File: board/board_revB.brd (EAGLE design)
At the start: 94 x 44.5 mm, 81 parts, among them Q2 ULN2003AD, Y1 8Mhz

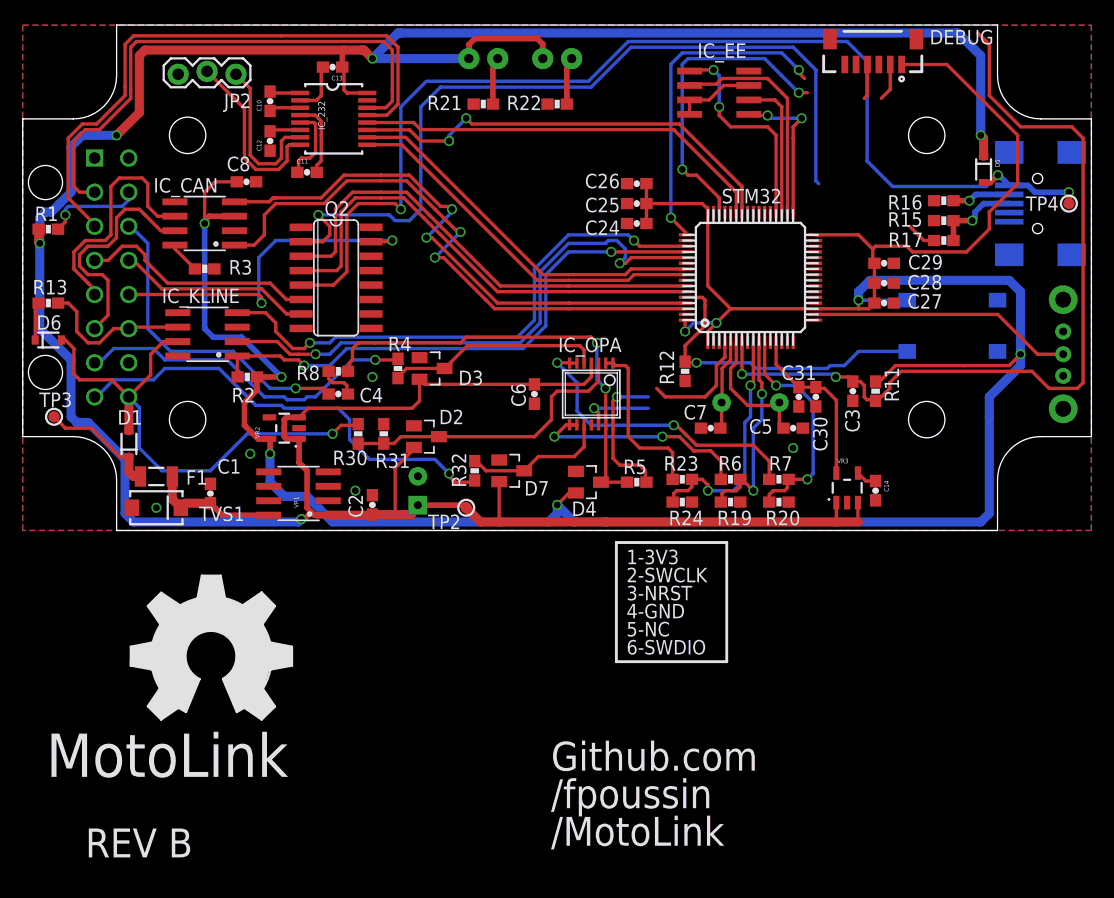
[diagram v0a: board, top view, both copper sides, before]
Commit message: [Board] working on rev B (routing)
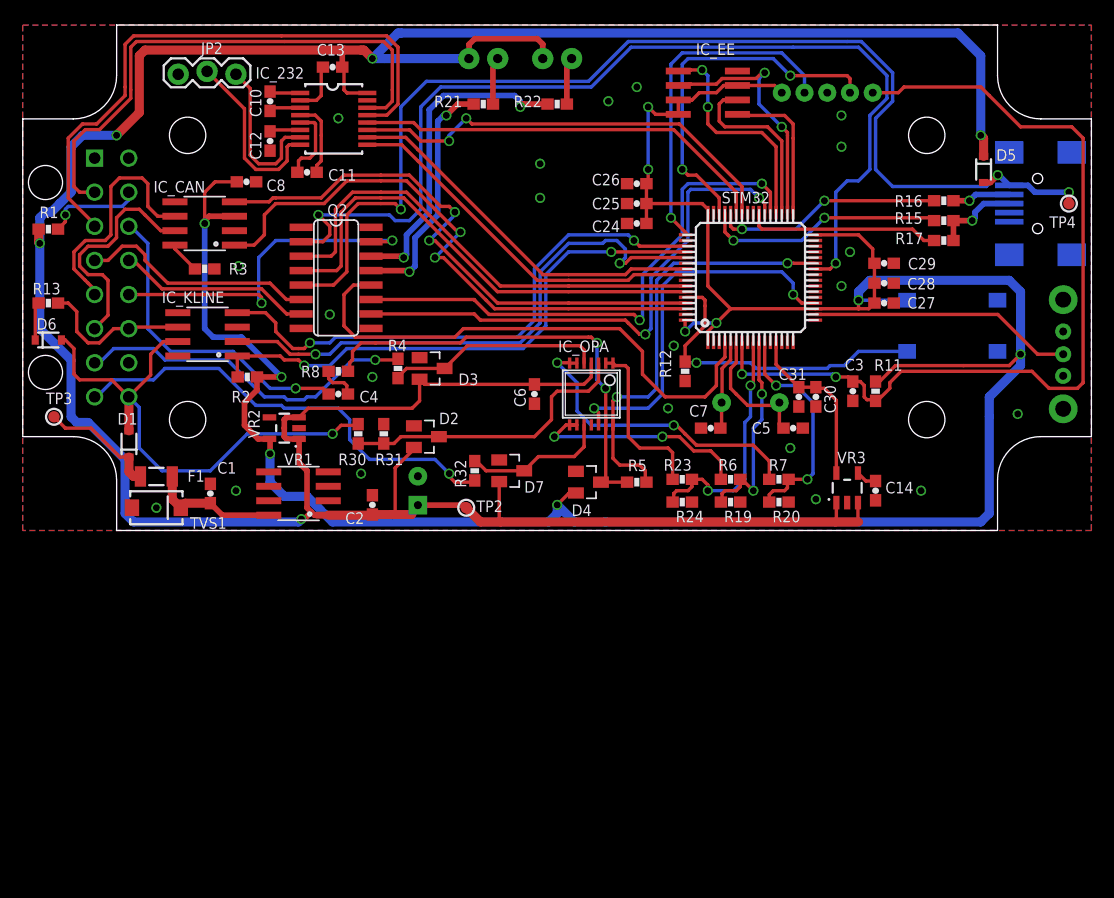
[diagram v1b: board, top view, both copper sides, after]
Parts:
- removed CON_DBG: JST_VERTICAL, SparkFun-Connectors:JST-6-SMD-VERT-1.0MM
- added JP4: (no value), SparkFun-Connectors:JST-5-PTH
- moved U$6 52.1 mm to (40.0, 25.6), flipped to the bottom
- moved IC_EE 1.00 mm to (60.2, 38.5)
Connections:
- removed net SWO: CON_DBG.6
- net +3V3: now also JP4.5; no longer CON_DBG.1
- net GND: now also JP4.3; no longer CON_DBG.3
- net NRST: now also JP4.1; no longer CON_DBG.5
- net SWCLK: now also JP4.4; no longer CON_DBG.2
- net SWDIO: now also JP4.2; no longer CON_DBG.4
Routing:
- net FREQ1_IN: track 0.00 -> 47.5 mm, vias 0 -> 2
- net FREQ2_IN: track 0.00 -> 47.1 mm, vias 0 -> 2
- net USB_DETECT: track 10.1 -> 47.1 mm
- net N$15: track 0.00 -> 28.6 mm, vias 0 -> 2
- net DAC1: track 6.38 -> 33.3 mm, vias 1 -> 2
- net KNK_AN: track 12.6 -> 37.8 mm, vias 1 -> 2
- net N$11: track 0.00 -> 21.5 mm, vias 0 -> 2
- net USB_DP: track 0.00 -> 21.3 mm, vias 0 -> 2
- net USB_DM: track 0.00 -> 20.2 mm, vias 0 -> 2
- net +3V3: track 254.4 -> 234.8 mm, vias 8 -> 10
- net SCS_TRIG: track 71.4 -> 88.7 mm, vias 1 -> 2
- net USB_CTRL: track 2.67 -> 17.1 mm
- net NRST: track 73.8 -> 78.6 mm
- net SPI2_MISO: track 12.5 -> 15.8 mm
- net SWCLK: track 32.1 -> 30.0 mm, vias 2 -> 1
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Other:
- board text removed: "1-3V3"
- board text removed: "2-SWCLK"
- board text removed: "3-NRST"
- board text removed: "4-GND"
- board text removed: "5-NC"
- board text removed: "6-SWDIO"

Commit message: [Board] working on rev B (routing/schema)
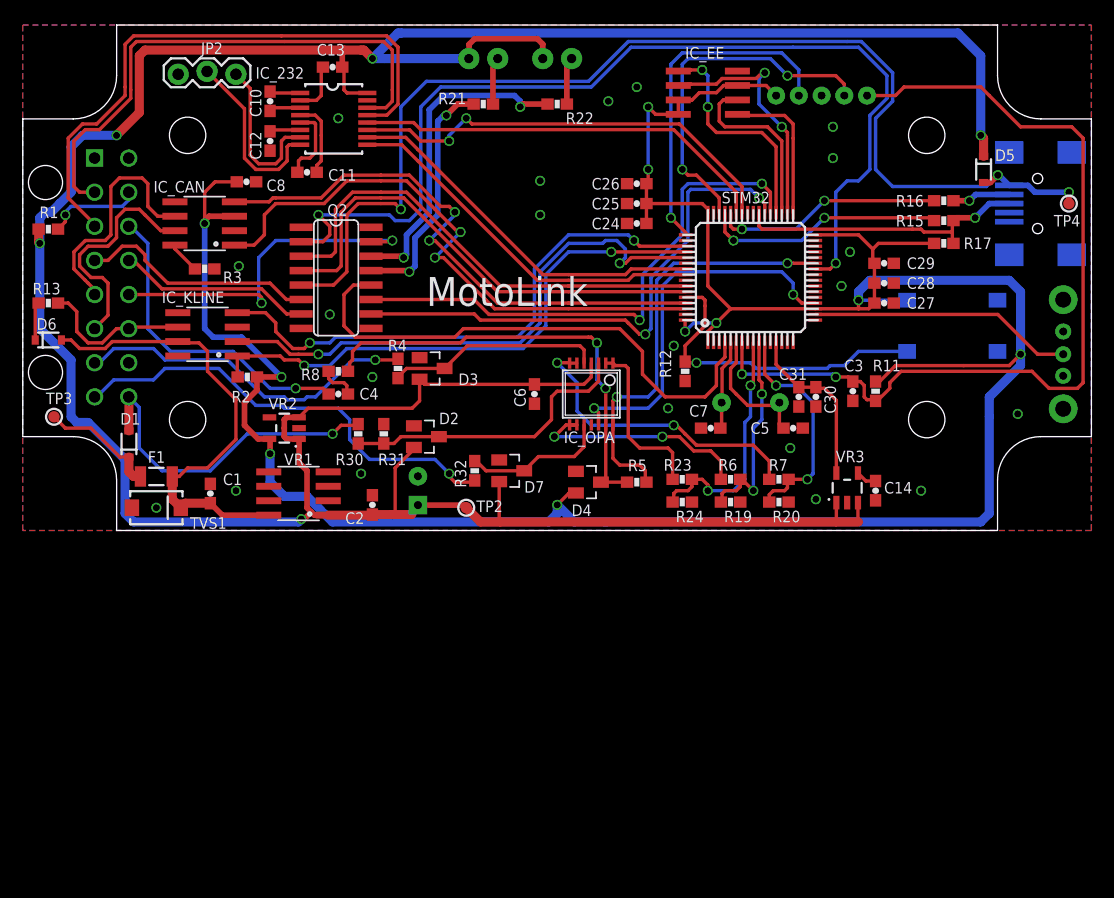
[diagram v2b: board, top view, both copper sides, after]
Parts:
- C9: value 47uF 25v -> 100uF 16v
- IC_KLINE: value MCP2004 -> TJA1027
- moved JP4 0.56 mm to (70.2, 38.2)
- moved R17 0.25 mm to (81.0, 25.2)
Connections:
- removed net N$7: JP1.D+, R15.1, R17.2
- net +12V: no longer D6.2, IC_KLINE.7
- net +3V3: now also R17.1
- net USB_CTRL: now also JP1.D+, R15.1, R17.2; no longer R17.1
- net VCC_PROT: now also D6.2, IC_KLINE.7
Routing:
- net VCC_PROT: track 11.4 -> 40.9 mm
- net +12V: track 46.4 -> 29.7 mm
- net USB_CTRL: track 17.1 -> 26.2 mm, vias 0 -> 1
- net N$7: track 7.56 -> 0.00 mm, vias 1 -> 0
- net +3V3: track 234.8 -> 240.0 mm
- net NRST: track 78.6 -> 79.2 mm
- net SWDIO: track 31.8 -> 31.2 mm
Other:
- board text added: "BOOT0"

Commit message: [Board] working on rev B (routing)
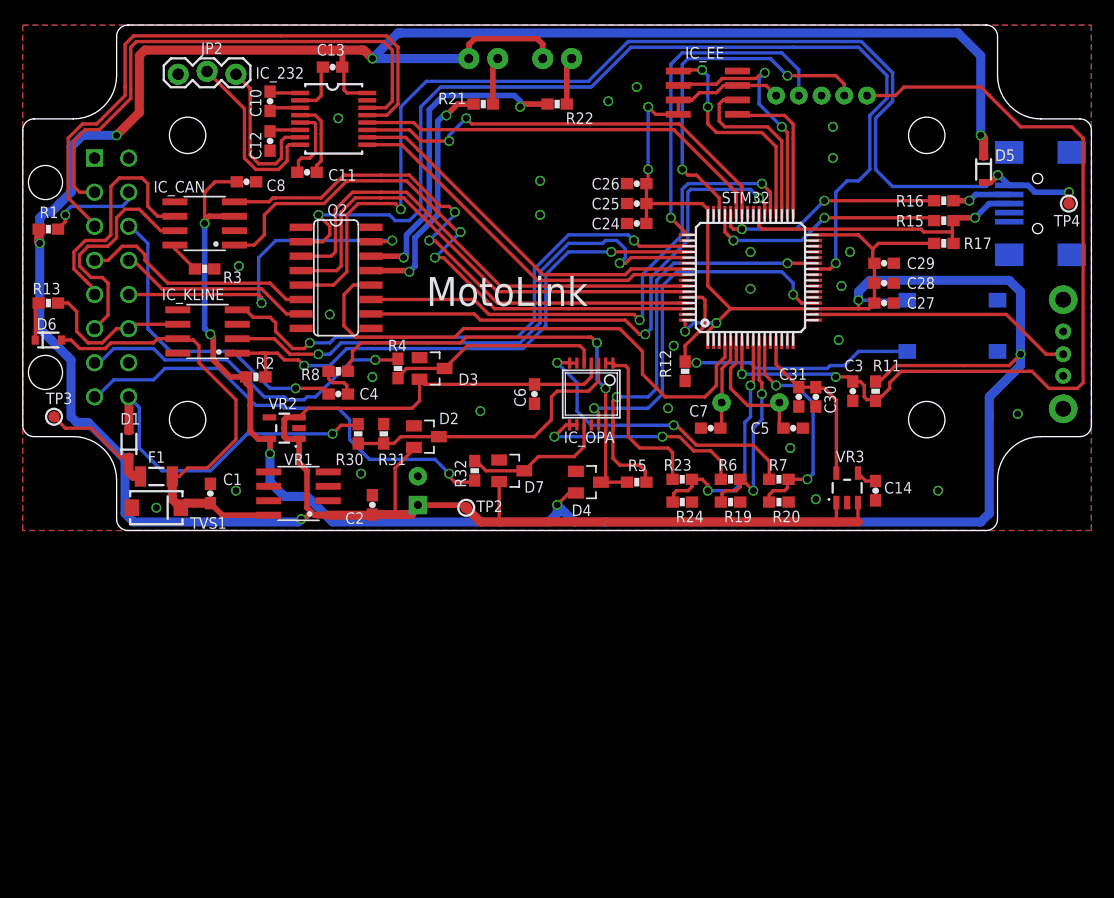
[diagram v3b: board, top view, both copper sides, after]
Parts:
- moved R2 0.75 mm to (20.5, 13.5), turned to 180 degrees
- moved IC_KLINE 0.25 mm to (16.2, 17.5)
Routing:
- net +3V3: track 240.0 -> 235.4 mm
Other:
- outline, holes or cut-outs redrawn

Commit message: [Board] working on rev B (routing/cleaning)
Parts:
- removed S2: EG1213, adafruit:EG1213
- added S3: (no value), SparkFun-Electromechanical:TACTILE-PTH-SIDEEZ
- JP1: value USBSMD -> USB-B; device SparkFun-Connectors:USB-MINIB -> SparkFun-Connectors:USB-B-PTH
- moved JP4 12.0 mm to (58.2, 38.2)
- moved IC_EE 9.28 mm to (69.5, 37.8)
- moved S1 6.27 mm to (75.5, 17.5)
- moved TP4 4.61 mm to (91.0, 24.2)
- moved JP1 3.95 mm to (86.0, 26.5)
- moved R3 1.03 mm to (17.0, 23.2)
- moved D3 0.25 mm to (36.0, 14.0)
- moved R21 0.25 mm to (40.5, 37.8)
- moved R22 0.25 mm to (47.0, 37.8)
- moved R4 0.25 mm to (33.0, 14.0)
- flipped LED1 to the top, turned to 0 degrees
- flipped LED2 to the top, turned to 0 degrees
- renumbered JP2 to CON_RS232
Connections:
- new net VCC_DETECT: Q2.16, STM32.57
- net BUT1: now also S3.1; no longer S2.2
- net GND: now also S3.2; no longer S2.3
- net VCC_PROT: now also Q2.1
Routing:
- net VCC_DETECT: track 0.00 -> 33.2 mm, vias 0 -> 2
- net NRST: track 79.2 -> 97.9 mm
- net VCC_PROT: track 41.0 -> 59.3 mm, vias 0 -> 2
- net SWDIO: track 31.2 -> 13.0 mm, vias 2 -> 1
- net SWCLK: track 30.1 -> 13.1 mm
- net SPI2_SCK: track 21.6 -> 13.4 mm
- net +5V: track 281.0 -> 273.5 mm
- net BOOT0: track 28.3 -> 22.1 mm
- net SPI2_MOSI: track 19.7 -> 13.9 mm
- net USB_VBUS: track 100.9 -> 105.4 mm, vias 3 -> 2
- net +3V3: track 235.4 -> 231.2 mm, vias 10 -> 9
- net SPI2_MISO: track 15.8 -> 12.4 mm
- net SPI2_NSS: track 13.0 -> 9.70 mm
- net BUT1: track 23.2 -> 25.9 mm
- net N$17: track 5.13 -> 2.69 mm, vias 1 -> 0
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
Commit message: [Board] working on rev B (routing/cleaning)
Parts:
- flipped CON_RS232 to the bottom, turned to 0 degrees
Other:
- board text added: "GND"
- board text added: "RS232"
- board text added: "RX"
- board text added: "TX"
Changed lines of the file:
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@@
 <text x="77.75" y="21.25" size="1.016" layer="26" font="vector" ratio="12" rot="MR0">BOOT0</text>
 <text x="32.5" y="18.5" size="3.81" layer="25" font="vector" ratio="12">MotoLink</text>
+<text x="14.75" y="42" size="1.016" layer="22" font="vector" ratio="12" rot="MR0">GND</text>
+<text x="17" y="42" size="1.016" layer="22" font="vector" ratio="12" rot="MR0">RX</text>
+<text x="19.75" y="42" size="1.016" layer="22" font="vector" ratio="12" rot="MR0">TX</text>
+<text x="20.5" y="40.75" size="1.016" layer="22" font="vector" ratio="12" rot="MR180">RS232</text>
 </plain>
 <attributes>
@@
 </element>
 <element name="IC_232" library="SparkFun-DigitalIC" package="TSSOP16" value="MAX202" x="27.25" y="36.25" locked="yes" smashed="yes" rot="R270">
-<attribute name="NAME" x="20.476" y="39.73" size="1.016" layer="25" font="vector" ratio="12"/>
+<attribute name="NAME" x="29.226" y="39.73" size="1.016" layer="25" font="vector" ratio="12"/>
 <attribute name="VALUE" x="28.139" y="37.774" size="0.6096" layer="27" rot="R270"/>
 </element>
@@
 </element>
 <element name="X2" library="con-molex-micro-fit-3_0" package="43045-1600" value="" x="2" y="22.25" locked="yes" smashed="yes" rot="MR90"/>
-<element name="CON_RS232" library="SparkFun-Connectors" package="1X03_LOCK" value="" x="18.75" y="40.25" smashed="yes" rot="R180">
-<attribute name="NAME" x="12.1538" y="42.0788" size="1.016" layer="25" font="vector" ratio="12"/>
-<attribute name="VALUE" x="20.02" y="43.425" size="1.27" layer="27" rot="R180"/>
+<element name="CON_RS232" library="SparkFun-Connectors" package="1X03_LOCK" value="" x="18.75" y="40.25" smashed="yes" rot="MR0">
+<attribute name="VALUE" x="20.02" y="37.075" size="1.27" layer="28" rot="MR0"/>
 </element>
 <element name="D5" library="SparkFun-DiscreteSemi" package="SOD-323" value="BAT165" x="84.5" y="31.75" smashed="yes" rot="R270">
@@
 <wire x1="69.7" y1="19.5" x2="62.25" y2="19.5" width="0.3" layer="1"/>
 <wire x1="62.25" y1="19.5" x2="61" y2="18.25" width="0.3" layer="1"/>
-<wire x1="54.85" y1="30.5" x2="54.85" y2="28.75" width="0.3" layer="1"/>
-<wire x1="54.85" y1="27" x2="54.85" y2="28.75" width="0.3" layer="1"/>
+<wire x1="54.85" y1="30.5" x2="54.85" y2="28.75" width="0.5" layer="1"/>
+<wire x1="54.85" y1="27" x2="54.85" y2="28.75" width="0.5" layer="1"/>
 <wire x1="60.25" y1="27.95" x2="60.25" y2="28.25" width="0.3" layer="1"/>
 <wire x1="60.25" y1="28.25" x2="59.75" y2="28.75" width="0.3" layer="1"/>
@@
 <wire x1="60.25" y1="27.95" x2="60.25" y2="21.5" width="0.3" layer="1"/>
 <wire x1="60.25" y1="21.5" x2="62.25" y2="19.5" width="0.3" layer="1"/>
-<wire x1="55" y1="36.5" x2="55" y2="31.75" width="0.3" layer="16"/>
+<wire x1="55" y1="36.5" x2="55" y2="31.75" width="0.5" layer="16"/>
 <via x="55" y="31.75" extent="1-16" drill="0.6"/>
-<wire x1="55" y1="31.75" x2="55" y2="30.65" width="0.3" layer="1"/>
+<wire x1="55" y1="31.75" x2="55" y2="30.65" width="0.5" layer="1"/>
 <wire x1="55" y1="30.65" x2="54.85" y2="30.5" width="0.3" layer="1"/>
 <contactref element="JP4" pad="5"/>
@@
 <wire x1="20.5" y1="31.75" x2="19.5" y2="32.75" width="0.3" layer="1"/>
 <wire x1="19.5" y1="32.75" x2="19.5" y2="37.087" width="0.3" layer="1"/>
-<wire x1="19.5" y1="37.087" x2="16.21" y2="40.377" width="0.3" layer="1"/>
+<wire x1="16.21" y1="40.123" x2="16.464" y2="40.123" width="0.3" layer="1"/>
+<wire x1="16.464" y1="40.123" x2="19.5" y2="37.087" width="0.3" layer="1"/>
 </signal>
 <signal name="UART2_TXD_232">
@@
 <wire x1="20.75" y1="32.25" x2="20" y2="33" width="0.3" layer="1"/>
 <wire x1="20" y1="33" x2="20" y2="38.873" width="0.3" layer="1"/>
-<wire x1="20" y1="38.873" x2="18.75" y2="40.123" width="0.3" layer="1"/>
+<wire x1="18.75" y1="40.377" x2="18.75" y2="40.123" width="0.3" layer="1"/>
+<wire x1="18.75" y1="40.123" x2="20" y2="38.873" width="0.3" layer="1"/>
 </signal>
 <signal name="UART3_TX">

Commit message: [Board] working on rev B (routing/cleaning)
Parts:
- removed JP4: (no value), SparkFun-Connectors:JST-5-PTH
- added X1: JST-ZH, con-jst:S4B-ZR
- moved C27 1.50 mm to (74.2, 20.0)
- moved C28 1.50 mm to (74.2, 21.8)
- moved C29 1.50 mm to (74.2, 23.5)
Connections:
- net +3V3: no longer JP4.5
- net GND: now also X1.2; no longer JP4.3
- net NRST: now also X1.4; no longer JP4.1
- net SWCLK: now also X1.1; no longer JP4.4
- net SWDIO: now also X1.3; no longer JP4.2
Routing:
- net SWCLK: track 13.1 -> 14.6 mm
- net SWDIO: track 13.0 -> 14.1 mm
- net +3V3: track 231.2 -> 230.8 mm, vias 9 -> 10

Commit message: [Board] working on rev B (routing/cleaning)
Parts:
- IC_EE: value FM25L04B -> FM25L04B/AT24C256
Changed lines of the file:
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@@
 <attribute name="PROD_ID" value="RES-11150" x="11.75" y="4.75" size="1.778" layer="27" rot="R180" display="off"/>
 </element>
-<element name="IC_EE" library="microchip" package="SO-08" value="FM25L04B" x="69.5" y="37.75" smashed="yes" rot="R90">
+<element name="IC_EE" library="microchip" package="SO-08" value="FM25L04B/AT24C256" x="69.5" y="37.75" locked="yes" smashed="yes" rot="R90">
 <attribute name="OC_NEWARK" value="96K4092" x="69.5" y="37.75" size="1.778" layer="27" rot="R90" display="off"/>
 <attribute name="MPN" value="25LC080/SN" x="69.5" y="37.75" size="1.778" layer="27" rot="R90" display="off"/>

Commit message: [Code] Updating mx2board script config
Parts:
- IC_EE: value FM25L04B/AT24C256 -> FM25L04B/25HP256
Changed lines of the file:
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@@
 <attribute name="PROD_ID" value="RES-11150" x="11.75" y="4.75" size="1.778" layer="27" rot="R180" display="off"/>
 </element>
-<element name="IC_EE" library="microchip" package="SO-08" value="FM25L04B/AT24C256" x="69.5" y="37.75" locked="yes" smashed="yes" rot="R90">
+<element name="IC_EE" library="microchip" package="SO-08" value="FM25L04B/25HP256" x="69.5" y="37.75" locked="yes" smashed="yes" rot="R90">
 <attribute name="OC_NEWARK" value="96K4092" x="69.5" y="37.75" size="1.778" layer="27" rot="R90" display="off"/>
 <attribute name="MPN" value="25LC080/SN" x="69.5" y="37.75" size="1.778" layer="27" rot="R90" display="off"/>
